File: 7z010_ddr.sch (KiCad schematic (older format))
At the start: 50 parts, among them U1 DDR3, U2 xc7z010clg400

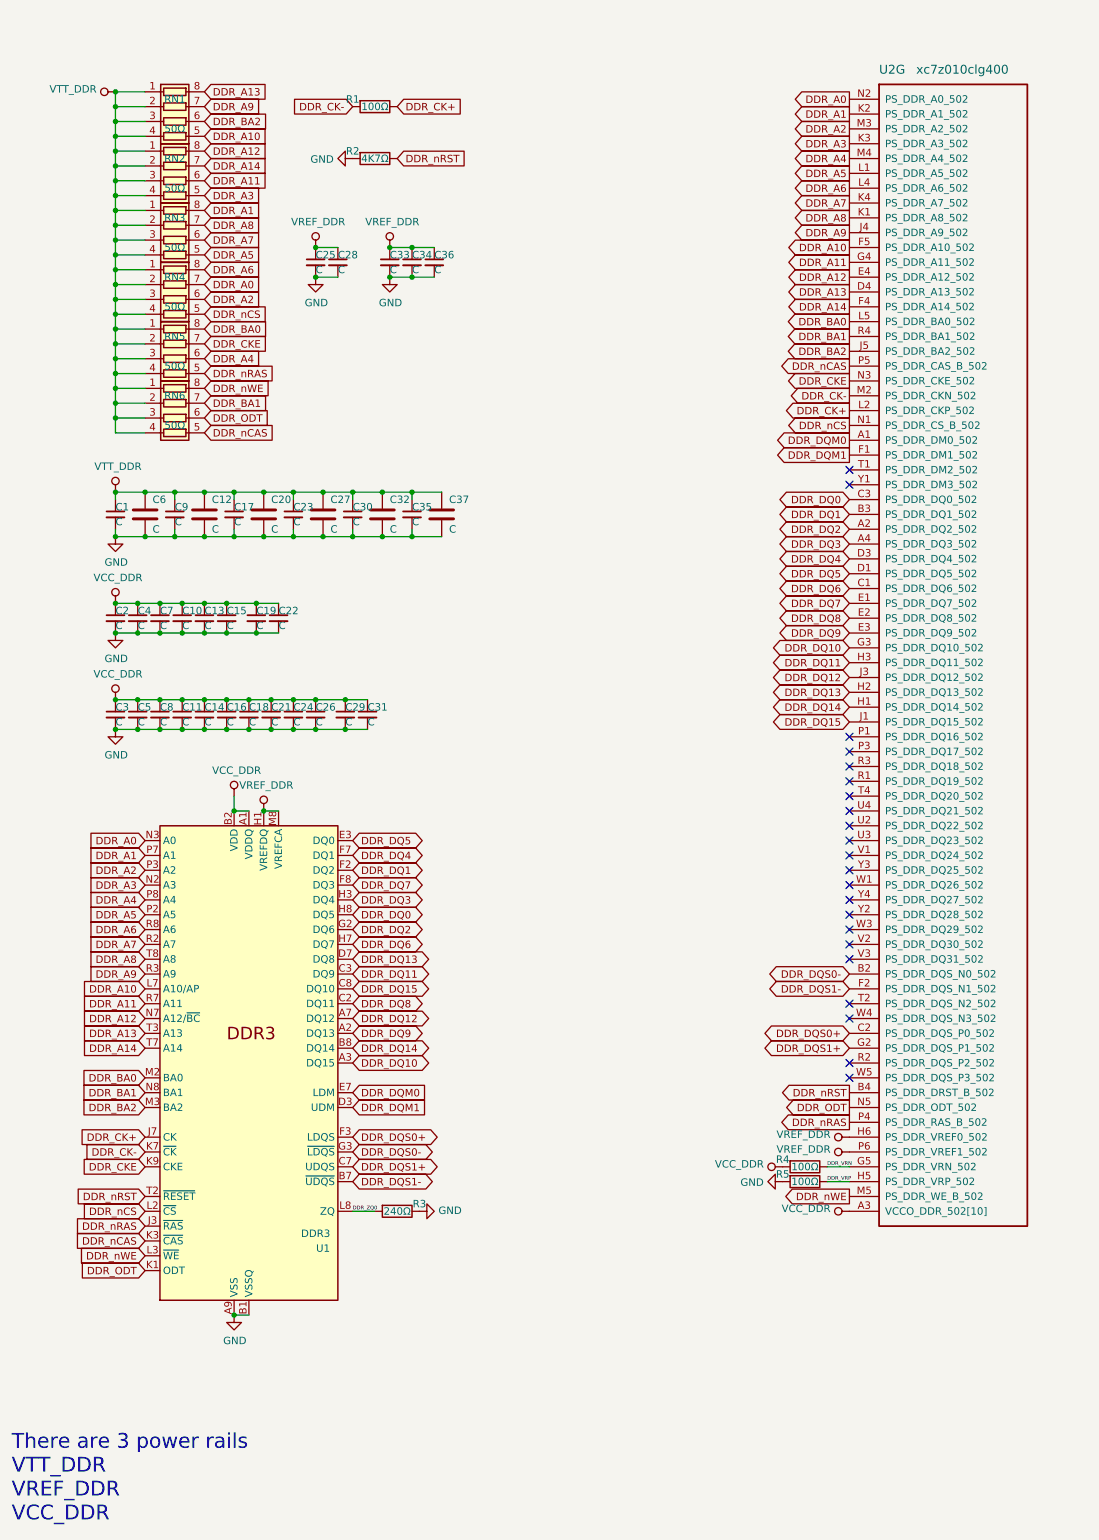
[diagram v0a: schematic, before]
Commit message: update termination resistor value
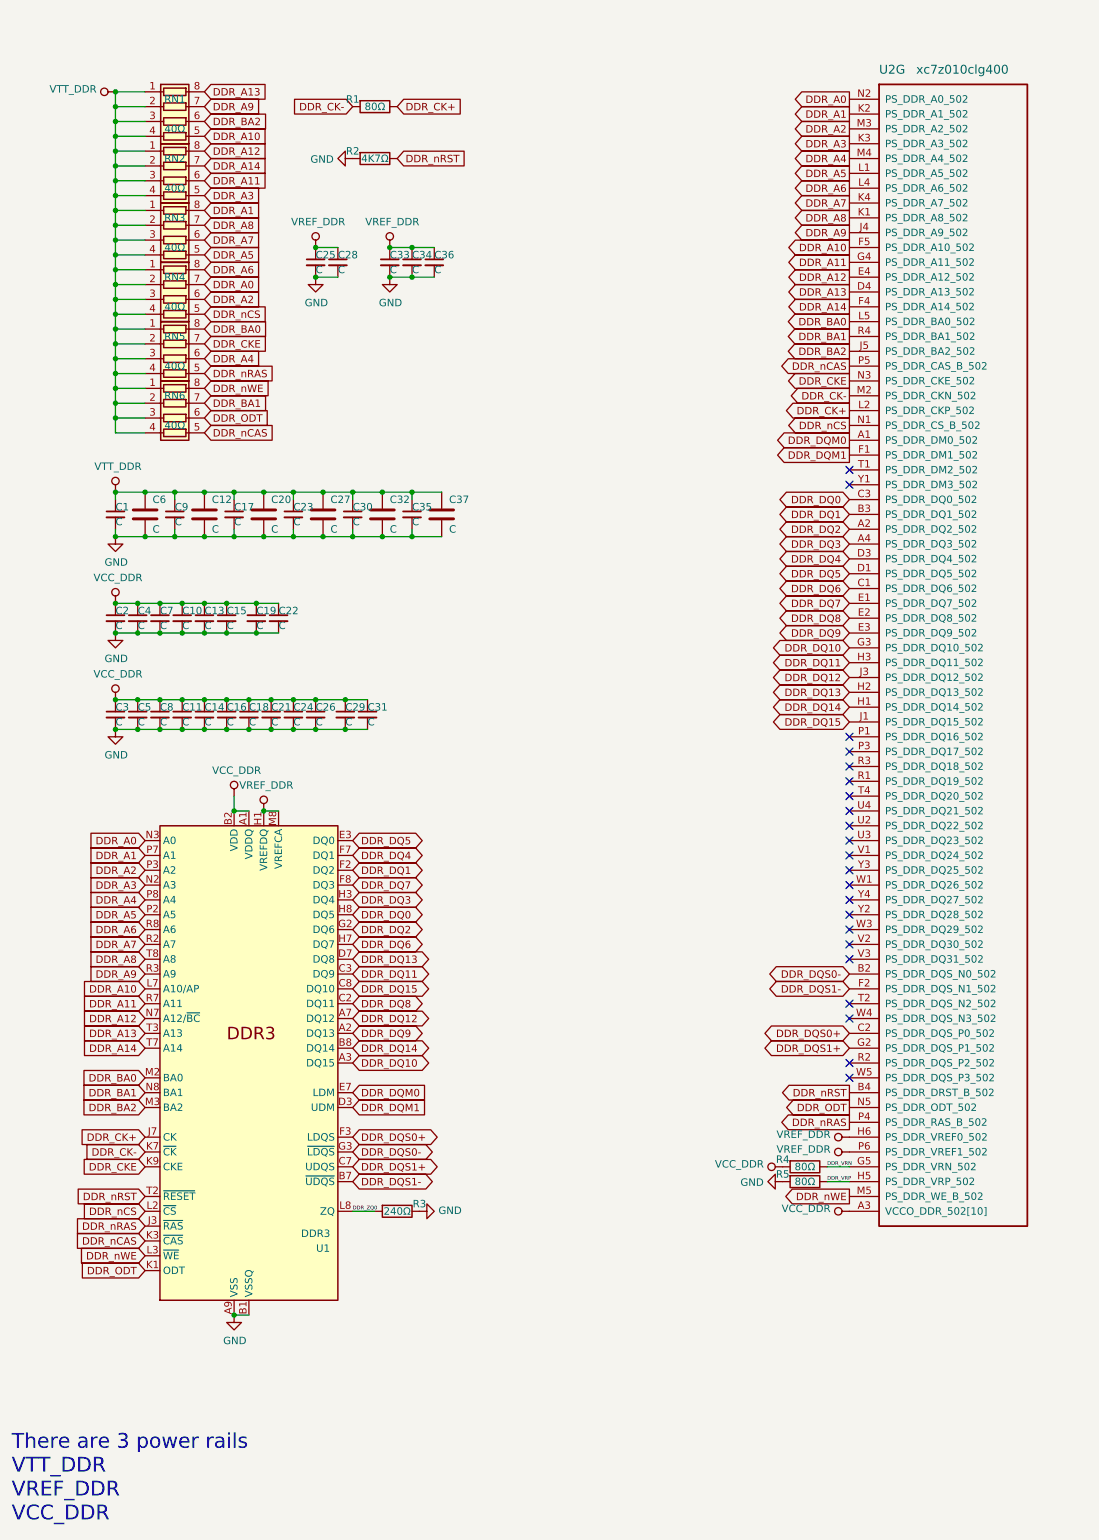
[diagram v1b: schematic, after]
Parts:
- R1, R4, R5: value 100Ω -> 80Ω
- RN1, RN2, RN3, RN4, RN5, RN6: value 50Ω -> 40Ω
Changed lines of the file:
@@
 P 5950 8100
 F 0 "R4" V 5900 7950 50  0000 C CNN
-F 1 "100Ω" V 5950 8100 50  0000 C CNN
+F 1 "80Ω" V 5950 8100 50  0000 C CNN
 F 2 "Resistor_SMD:R_0201_0603Metric" V 5880 8100 50  0001 C CNN
 F 3 "~" H 5950 8100 50  0001 C CNN
@@
 P 5950 8200
 F 0 "R5" V 5900 8050 50  0000 C CNN
-F 1 "100Ω" V 5950 8200 50  0000 C CNN
+F 1 "80Ω" V 5950 8200 50  0000 C CNN
 F 2 "Resistor_SMD:R_0201_0603Metric" V 5880 8200 50  0001 C CNN
 F 3 "~" H 5950 8200 50  0001 C CNN
@@
 P 3050 950
 F 0 "R1" V 3000 800 50  0000 C CNN
-F 1 "100Ω" V 3050 950 50  0000 C CNN
+F 1 "80Ω" V 3050 950 50  0000 C CNN
 F 2 "Resistor_SMD:R_0201_0603Metric" V 2980 950 50  0001 C CNN
 F 3 "~" H 3050 950 50  0001 C CNN
@@
 P 1700 1050
 F 0 "RN1" V 1550 1050 50  0000 C CNN
-F 1 "50Ω" V 1750 1050 50  0000 C CNN
+F 1 "40Ω" V 1750 1050 50  0000 C CNN
 F 2 "Resistor_SMD:R_Array_Convex_4x0402" V 1975 1050 50  0001 C CNN
 F 3 "~" H 1700 1050 50  0001 C CNN
@@
 P 1700 1450
 F 0 "RN2" V 1550 1450 50  0000 C CNN
-F 1 "50Ω" V 1750 1450 50  0000 C CNN
+F 1 "40Ω" V 1750 1450 50  0000 C CNN
 F 2 "Resistor_SMD:R_Array_Convex_4x0402" V 1975 1450 50  0001 C CNN
 F 3 "~" H 1700 1450 50  0001 C CNN
@@
 P 1700 1850
 F 0 "RN3" V 1550 1850 50  0000 C CNN
-F 1 "50Ω" V 1750 1850 50  0000 C CNN
+F 1 "40Ω" V 1750 1850 50  0000 C CNN
 F 2 "Resistor_SMD:R_Array_Convex_4x0402" V 1975 1850 50  0001 C CNN
 F 3 "~" H 1700 1850 50  0001 C CNN
@@
 P 1700 2250
 F 0 "RN4" V 1550 2250 50  0000 C CNN
-F 1 "50Ω" V 1750 2250 50  0000 C CNN
+F 1 "40Ω" V 1750 2250 50  0000 C CNN
 F 2 "Resistor_SMD:R_Array_Convex_4x0402" V 1975 2250 50  0001 C CNN
 F 3 "~" H 1700 2250 50  0001 C CNN
@@
 P 1700 2650
 F 0 "RN5" V 1550 2650 50  0000 C CNN
-F 1 "50Ω" V 1750 2650 50  0000 C CNN
+F 1 "40Ω" V 1750 2650 50  0000 C CNN
 F 2 "Resistor_SMD:R_Array_Convex_4x0402" V 1975 2650 50  0001 C CNN
 F 3 "~" H 1700 2650 50  0001 C CNN
@@
 P 1700 3050
 F 0 "RN6" V 1550 3050 50  0000 C CNN
-F 1 "50Ω" V 1750 3050 50  0000 C CNN
+F 1 "40Ω" V 1750 3050 50  0000 C CNN
 F 2 "Resistor_SMD:R_Array_Convex_4x0402" V 1975 3050 50  0001 C CNN
 F 3 "~" H 1700 3050 50  0001 C CNN

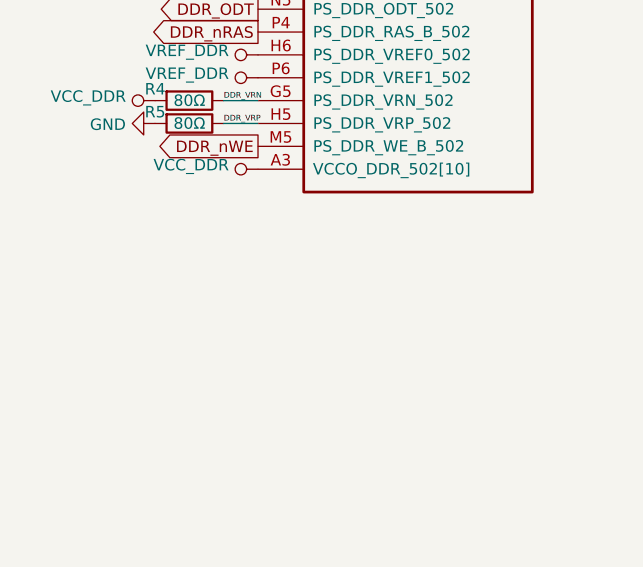
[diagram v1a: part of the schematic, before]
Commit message: added GND back to sch
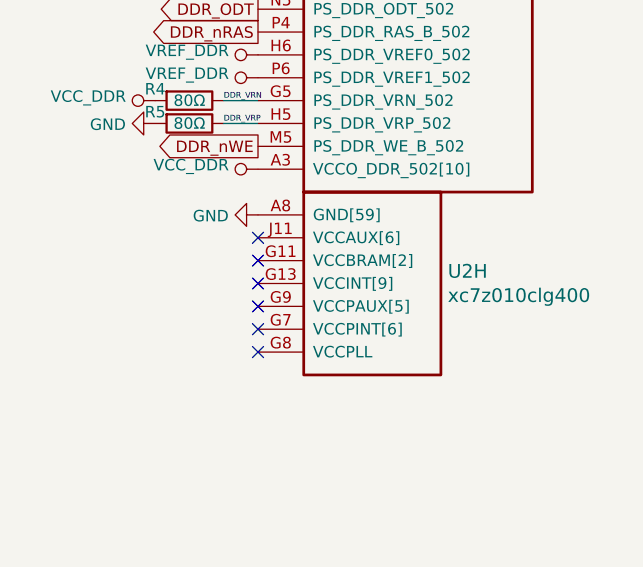
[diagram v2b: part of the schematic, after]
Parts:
- added unit 8 of U2
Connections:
- net GND: now also U2.A18 (GND[59]), U2.A8 (GND[59]), U2.B1 (GND[59]), U2.B11 (GND[59]), U2.C14 (GND[59]), U2.C4 (GND[59]), U2.C9 (GND[59]), U2.D17 (GND[59]), U2.E10 (GND[59]), U2.E20 (GND[59]), U2.F3 (GND[59]), U2.F7 (GND[59]), U2.G10 (GND[59]), U2.G12 (GND[59]), U2.G16 (GND[59]), U2.H11 (GND[59]), U2.H13 (GND[59]), U2.H19 (GND[59]), U2.H7 (GND[59]), U2.H9 (GND[59]), U2.J12 (GND[59]), U2.J2 (GND[59]), U2.J8 (GND[59]), U2.K11 (GND[59]), U2.K13 (GND[59]), U2.K15 (GND[59]), U2.K5 (GND[59]), U2.K7 (GND[59]), U2.L12 (GND[59]), U2.L18 (GND[59]), U2.L8 (GND[59]), U2.M1 (GND[59]), U2.M11 (GND[59]), U2.M13 (GND[59]), U2.M7 (GND[59]), U2.N10 (GND[59]), U2.N12 (GND[59]), U2.N14 (GND[59]), U2.N4 (GND[59]), U2.N8 (GND[59]), U2.P11 (GND[59]), U2.P13 (GND[59]), U2.P17 (GND[59]), U2.P7 (GND[59]), U2.P9 (GND[59]), U2.R12 (GND[59]), U2.R20 (GND[59]), U2.R8 (GND[59]), U2.T13 (GND[59]), U2.T3 (GND[59]), U2.T7 (GND[59]), U2.U16 (GND[59]), U2.U6 (GND[59]), U2.V19 (GND[59]), U2.V9 (GND[59]), U2.W12 (GND[59]), U2.W2 (GND[59]), U2.Y15 (GND[59]), U2.Y5 (GND[59])
- new net: U2.F8 (VCCPAUX[5]), U2.G9 (VCCPAUX[5]), U2.H8 (VCCPAUX[5]), U2.K8 (VCCPAUX[5]), U2.M8 (VCCPAUX[5])
- new net: U2.G11 (VCCBRAM[2]), U2.H10 (VCCBRAM[2])
- new net: U2.G13 (VCCINT[9]), U2.H12 (VCCINT[9]), U2.J13 (VCCINT[9]), U2.K12 (VCCINT[9]), U2.L13 (VCCINT[9]), U2.M12 (VCCINT[9]), U2.N13 (VCCINT[9]), U2.P12 (VCCINT[9]), U2.R13 (VCCINT[9])
- new net: U2.G7 (VCCPINT[6]), U2.J7 (VCCPINT[6]), U2.L7 (VCCPINT[6]), U2.N7 (VCCPINT[6]), U2.P8 (VCCPINT[6]), U2.R7 (VCCPINT[6])
- new net: U2.J11 (VCCAUX[6]), U2.L11 (VCCAUX[6]), U2.N11 (VCCAUX[6]), U2.N9 (VCCAUX[6]), U2.P10 (VCCAUX[6]), U2.R9 (VCCAUX[6])
- no-connect marks 22 -> 28
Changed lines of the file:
@@
 Text Notes 600  10500 0    100  ~ 0
 There are 3 power rails\nVTT_DDR\nVREF_DDR\nVCC_DDR
+$Comp
+L xilinx7:xc7z010clg400 U2
+U 8 1 619FCFE9
+P 6250 8600
+F 0 "U2" H 7080 8353 60  0000 L CNN
+F 1 "xc7z010clg400" H 7080 8247 60  0000 L CNN
+F 2 "" H 6450 8650 60  0001 L CNN
+F 3 "" H 6450 8450 60  0001 L CNN
+F 4 "xc7z010clg400" H 6450 8350 60  0001 L CNN "desc"
+	8    6250 8600
+	1    0    0    -1
+$EndComp
+$Comp
+L power:GND #PWR0101
+U 1 1 61A0FC06
+P 6250 8600
+F 0 "#PWR0101" H 6250 8350 50  0001 C CNN
+F 1 "GND" V 6255 8472 50  0000 R CNN
+F 2 "" H 6250 8600 50  0001 C CNN
+F 3 "" H 6250 8600 50  0001 C CNN
+	1    6250 8600
+	0    1    1    0
+$EndComp
+NoConn ~ 6250 8700
+NoConn ~ 6250 8800
+NoConn ~ 6250 8900
+NoConn ~ 6250 9000
+NoConn ~ 6250 9100
+NoConn ~ 6250 9200
 $EndSCHEMATC

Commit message: move symbols to project library
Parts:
- U1: symbol Memory_RAM:AS4C256M16D3 -> 7z010_ddr:AS4C256M16D3
- U2: symbol xilinx7:xc7z010clg400 -> 7z010_ddr:xc7z010clg400
- U2: footprint (none) -> Package_BGA:Xilinx_CLG400_NoPaste_JLC_Package_Delay
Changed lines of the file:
@@
 NoConn ~ 6250 3500
 $Comp
-L 7z010_ddr-rescue:VCC_DDR-power #PWR021
+L 7z010_ddr:VCC_DDR-power #PWR021
 U 1 1 614A8783
 P 6250 8400
@@
 $EndComp
 $Comp
-L 7z010_ddr-rescue:VCC_DDR-power #PWR017
+L 7z010_ddr:VCC_DDR-power #PWR017
 U 1 1 614B9E1D
 P 5800 8100
@@
 	2200 5700 2100 5700
 $Comp
-L 7z010_ddr-rescue:VCC_DDR-power #PWR08
+L 7z010_ddr:VCC_DDR-power #PWR08
 U 1 1 6148CC94
 P 2100 5600
@@
 DDR_CK+
 $Comp
-L Memory_RAM:AS4C256M16D3 U1
+L 7z010_ddr:AS4C256M16D3 U1
 U 1 1 615174BF
 P 2200 7400
@@
 	2900 8400 3050 8400
 $Comp
-L xilinx7:xc7z010clg400 U2
+L 7z010_ddr:xc7z010clg400 U2
 U 7 1 614B1DEB
 P 6250 900
@@
 $EndComp
 $Comp
-L 7z010_ddr-rescue:VREF_DDR-power #PWR019
+L 7z010_ddr:VREF_DDR-power #PWR019
 U 1 1 61654CD5
 P 6250 7900
@@
 $EndComp
 $Comp
-L 7z010_ddr-rescue:VREF_DDR-power #PWR020
+L 7z010_ddr:VREF_DDR-power #PWR020
 U 1 1 6165757C
 P 6250 8000
@@
 $EndComp
 $Comp
-L 7z010_ddr-rescue:VREF_DDR-power #PWR010
+L 7z010_ddr:VREF_DDR-power #PWR010
 U 1 1 6165797F
 P 2300 5700
@@
 	1    0    0    -1
 $EndComp
-Connection ~ 2300 5700
 Wire Wire Line
 	1500 850  1300 850
@@
 Wire Wire Line
 	1300 3150 1300 3050
-Connection ~ 1300 850
-$Comp
-L 7z010_ddr-rescue:VTT_DDR-power #PWR01
+$Comp
+L 7z010_ddr:VTT_DDR-power #PWR01
 U 1 1 6150C0BF
 P 1300 850
@@
 $EndComp
 $Comp
-L 7z010_ddr-rescue:VCC_DDR-power #PWR06
+L 7z010_ddr:VCC_DDR-power #PWR06
 U 1 1 6154A9DE
 P 1300 4950
@@
 Wire Wire Line
 	1300 4950 1450 4950
-Connection ~ 1300 4950
 Wire Wire Line
 	1300 5150 1450 5150
@@
 Connection ~ 1300 5150
 $Comp
-L 7z010_ddr-rescue:VREF_DDR-power #PWR014
+L 7z010_ddr:VREF_DDR-power #PWR014
 U 1 1 615E5283
 P 3150 1900
@@
 	3150 2100 3300 2100
 $Comp
-L 7z010_ddr-rescue:VTT_DDR-power #PWR02
+L 7z010_ddr:VTT_DDR-power #PWR02
 U 1 1 616C970F
 P 1300 3550
@@
 $EndComp
 $Comp
-L 7z010_ddr-rescue:VCC_DDR-power #PWR04
+L 7z010_ddr:VCC_DDR-power #PWR04
 U 1 1 617B0423
 P 1300 4300
@@
 Wire Wire Line
 	1300 4300 1450 4300
-Connection ~ 1300 4300
 Connection ~ 1450 4300
 Connection ~ 1600 4300
@@
 Connection ~ 1300 4500
 $Comp
-L 7z010_ddr-rescue:VREF_DDR-power #PWR011
+L 7z010_ddr:VREF_DDR-power #PWR011
 U 1 1 617DE011
 P 2650 1900
@@
 	1    0    0    -1
 $EndComp
-Connection ~ 3150 1900
 Connection ~ 3150 2100
-Connection ~ 2650 1900
 Connection ~ 2650 2100
 Text GLabel 1900 2150 2    50   Input ~ 0
@@
 Wire Wire Line
 	1300 3600 1300 3550
-Connection ~ 1300 3550
 Wire Wire Line
 	1300 3800 1300 3850
@@
 F 0 "U2" H 7080 8353 60  0000 L CNN
 F 1 "xc7z010clg400" H 7080 8247 60  0000 L CNN
-F 2 "" H 6450 8650 60  0001 L CNN
+F 2 "Package_BGA:Xilinx_CLG400_NoPaste_JLC_Package_Delay" H 6450 8650 60  0001 L CNN
 F 3 "" H 6450 8450 60  0001 L CNN
 F 4 "xc7z010clg400" H 6450 8350 60  0001 L CNN "desc"

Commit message: move symbols to project library
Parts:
- U2: symbol xilinx7:xc7z010clg400 -> 7z010_ddr:xc7z010clg400
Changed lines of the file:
@@
 There are 3 power rails\nVTT_DDR\nVREF_DDR\nVCC_DDR
 $Comp
-L xilinx7:xc7z010clg400 U2
+L 7z010_ddr:xc7z010clg400 U2
 U 8 1 619FCFE9
 P 6250 8600
